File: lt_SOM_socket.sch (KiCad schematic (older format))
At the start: 2 parts

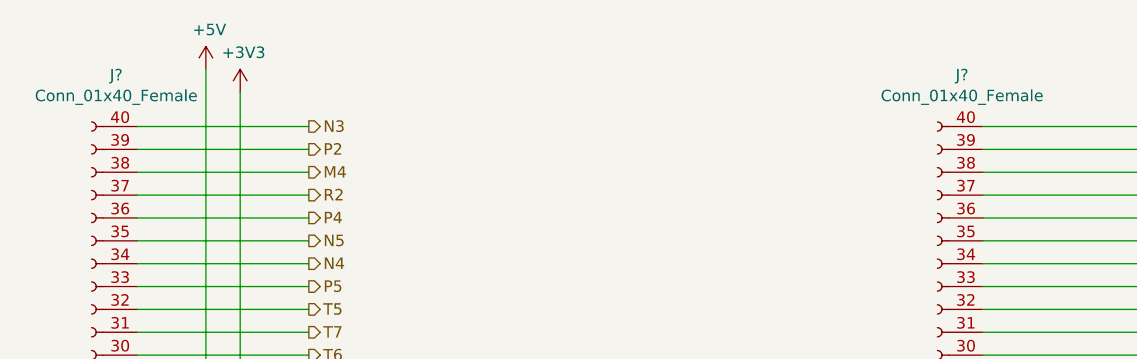
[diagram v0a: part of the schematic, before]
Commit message: Joystick net assigned.
Signed-off-by: Kali Prasad <kprasadvnsi@protonmail.com>
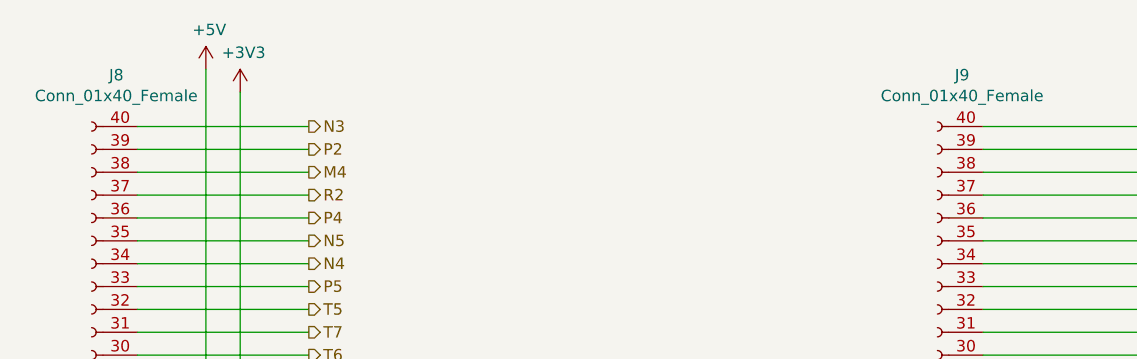
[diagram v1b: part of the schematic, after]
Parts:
- gave numbers to parts that had none: 2
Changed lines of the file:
@@
 $EndDescr
 $Comp
-L Connector:Conn_01x40_Female J?
+L Connector:Conn_01x40_Female J8
 U 1 1 5D31BC56
 P 1950 3850
-F 0 "J?" H 1842 1625 50  0000 C CNN
+F 0 "J8" H 1842 1625 50  0000 C CNN
 F 1 "Conn_01x40_Female" H 1842 1716 50  0000 C CNN
 F 2 "" H 1950 3850 50  0001 C CNN
@@
 $EndComp
 $Comp
-L Connector:Conn_01x40_Female J?
+L Connector:Conn_01x40_Female J9
 U 1 1 5D31DAE5
 P 5650 3850
-F 0 "J?" H 5542 1625 50  0000 C CNN
+F 0 "J9" H 5542 1625 50  0000 C CNN
 F 1 "Conn_01x40_Female" H 5542 1716 50  0000 C CNN
 F 2 "" H 5650 3850 50  0001 C CNN
@@
 	2150 5650 2900 5650
 $Comp
-L power:GND #PWR?
+L power:GND #PWR043
 U 1 1 5D4083AB
 P 5950 5900
-F 0 "#PWR?" H 5950 5650 50  0001 C CNN
+F 0 "#PWR043" H 5950 5650 50  0001 C CNN
 F 1 "GND" H 5955 5727 50  0000 C CNN
 F 2 "" H 5950 5900 50  0001 C CNN
@@
 	5950 4950 5950 5900
 $Comp
-L power:GND #PWR?
+L power:GND #PWR040
 U 1 1 5D41AB42
 P 2250 5900
-F 0 "#PWR?" H 2250 5650 50  0001 C CNN
+F 0 "#PWR040" H 2250 5650 50  0001 C CNN
 F 1 "GND" H 2255 5727 50  0000 C CNN
 F 2 "" H 2250 5900 50  0001 C CNN
@@
 NoConn ~ 2150 5150
 $Comp
-L power:+5V #PWR?
+L power:+5V #PWR041
 U 1 1 5D438DEB
 P 2450 1600
-F 0 "#PWR?" H 2450 1450 50  0001 C CNN
+F 0 "#PWR041" H 2450 1450 50  0001 C CNN
 F 1 "+5V" H 2465 1773 50  0000 C CNN
 F 2 "" H 2450 1600 50  0001 C CNN
@@
 	2150 5550 2450 5550
 $Comp
-L power:+3V3 #PWR?
+L power:+3V3 #PWR042
 U 1 1 5D44B72A
 P 2600 1700
-F 0 "#PWR?" H 2600 1550 50  0001 C CNN
+F 0 "#PWR042" H 2600 1550 50  0001 C CNN
 F 1 "+3V3" H 2615 1873 50  0000 C CNN
 F 2 "" H 2600 1700 50  0001 C CNN
